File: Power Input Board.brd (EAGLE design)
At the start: 136.7 x 125.3 mm, 17 parts, among them Q1 SPB80P06P

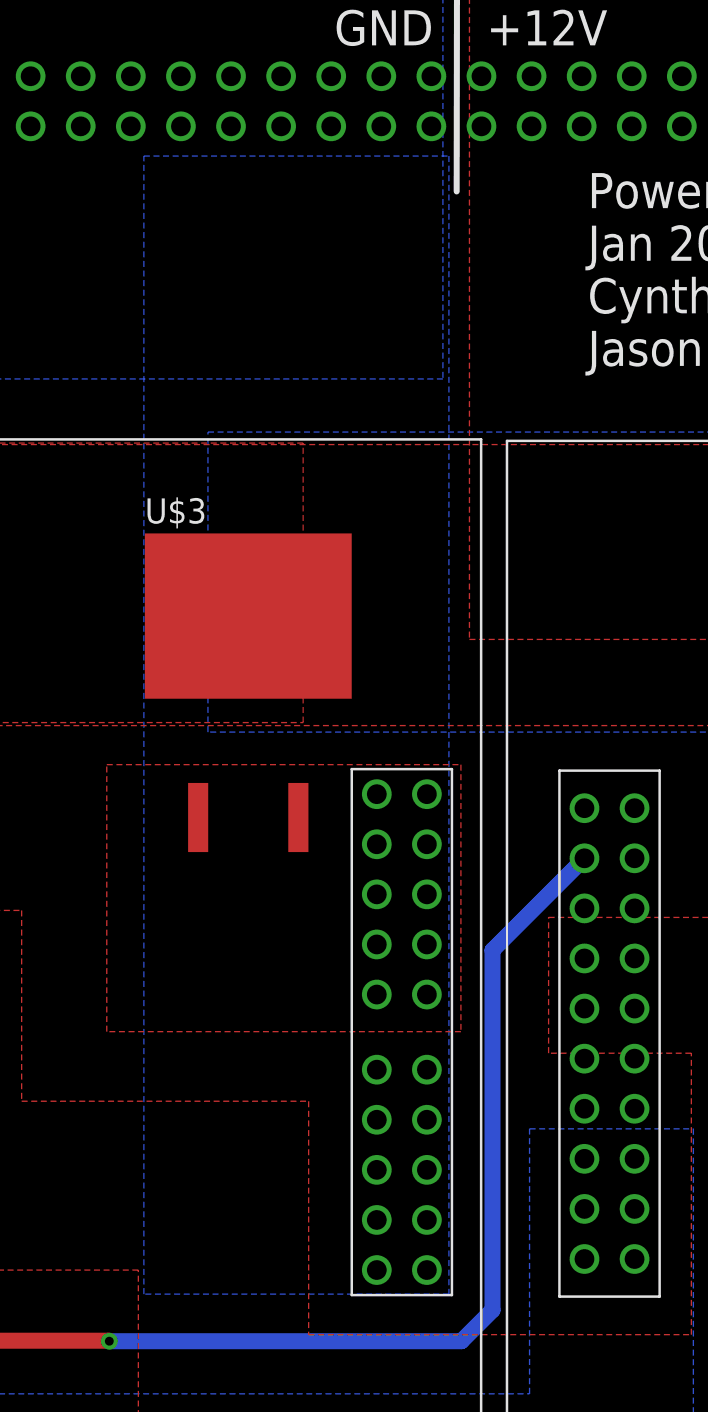
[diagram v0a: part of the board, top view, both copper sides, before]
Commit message: added LED
added LED between 12V and GND
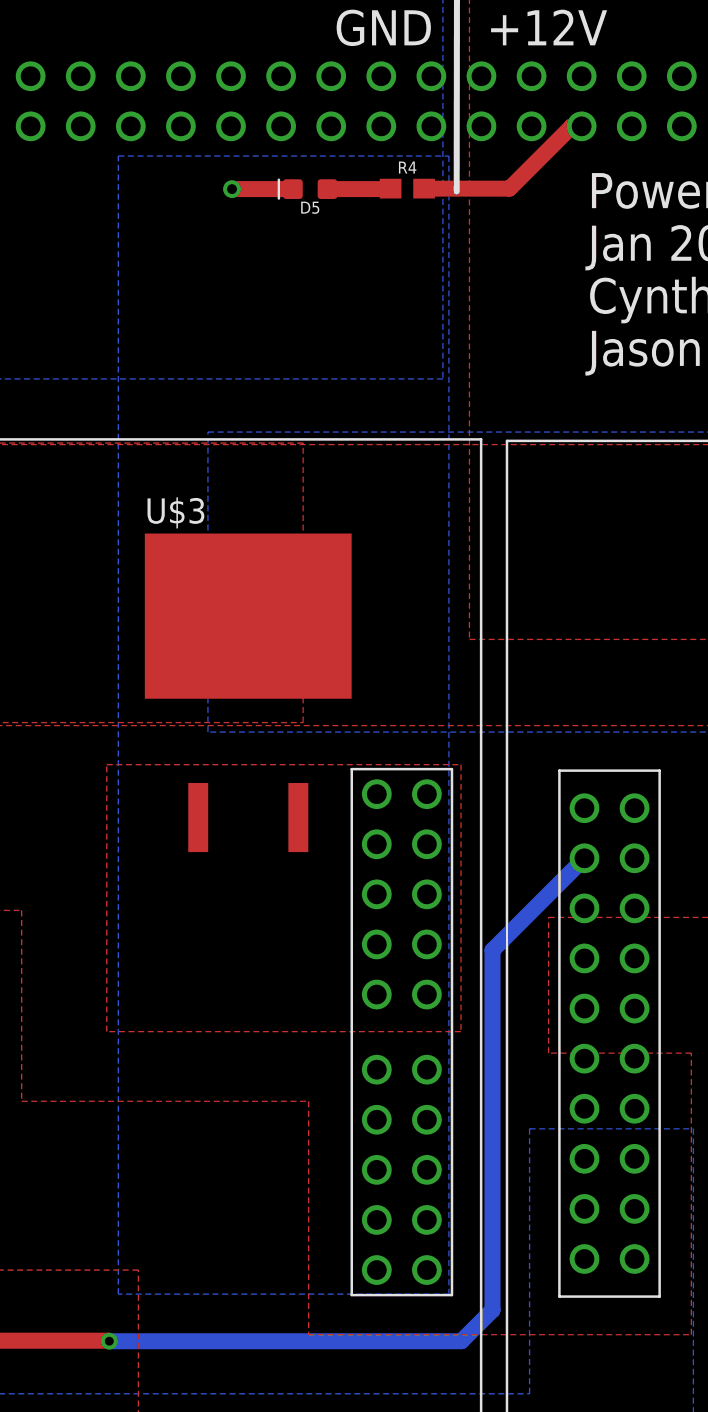
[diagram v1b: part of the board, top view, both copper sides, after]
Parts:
- added D5: (no value), SparkFun-LED:LED-0603
- added R4: 470, SparkFun-Resistors:0603
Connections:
- new net N$4: D5.A, R4.1
- net +12V: now also R4.2
- net GND: now also D5.C
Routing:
- net +12V: track 0.00 -> 9.30 mm
- net N$4: track 0.00 -> 3.21 mm
- net GND: track 0.00 -> 3.09 mm, vias 0 -> 1
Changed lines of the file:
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@@
 </element>
 <element name="U$7" library="PDB_PCB_connectors" package="PDB_PCB_2" value="PDB_PCB_CONNEC" x="0" y="0"/>
+<element name="D5" library="SparkFun-LED" library_urn="urn:adsk.eagle:library:529" package="LED-0603" package3d_urn="urn:adsk.eagle:package:39354/1" value="" x="59.3598" y="110.9472" rot="R180">
+<attribute name="NAME" x="59.3598" y="110.3122" size="0.6096" layer="25" font="vector" ratio="20" rot="R180" align="bottom-center"/>
+<attribute name="VALUE" x="59.3598" y="111.5822" size="0.6096" layer="27" font="vector" ratio="20" rot="R180" align="top-center"/>
+</element>
+<element name="R4" library="SparkFun-Resistors" library_urn="urn:adsk.eagle:library:532" package="0603" package3d_urn="urn:adsk.eagle:package:39650/1" value="470" x="64.2874" y="110.9726">
+<attribute name="NAME" x="64.2874" y="111.7346" size="0.6096" layer="25" font="vector" ratio="20" align="bottom-center"/>
+<attribute name="PROD_ID" value=" " x="64.2874" y="110.9726" size="1.778" layer="27" display="off"/>
+<attribute name="VALUE" x="64.2874" y="109.8296" size="0.6096" layer="27" font="vector" ratio="20" align="top-center"/>
+</element>
 </elements>
 <signals>
@@
 <vertex x="120.777" y="30.5562"/>
 </polygon>
+<contactref element="R4" pad="2"/>
+<wire x1="65.1374" y1="110.9726" x2="69.469" y2="110.9726" width="0.8128" layer="1"/>
+<wire x1="69.469" y1="110.9726" x2="72.6265625" y2="114.1301625" width="0.8128" layer="1"/>
+<wire x1="72.6265625" y1="114.1301625" x2="73.1260375" y2="114.1301625" width="0.8128" layer="1"/>
 </signal>
 <signal name="GND">
@@
 </polygon>
 <polygon width="0.8128" layer="16" isolate="0.8128">
-<vertex x="50.927" y="112.6236"/>
+<vertex x="49.6316" y="112.6236"/>
 <vertex x="66.3956" y="112.6236"/>
 <vertex x="66.3956" y="54.9148"/>
-<vertex x="50.927" y="54.9148"/>
+<vertex x="49.6316" y="54.9148"/>
 </polygon>
 <polygon width="0.8128" layer="16" isolate="0.8128">
@@
 <vertex x="28.0924" y="82.6516"/>
 </polygon>
+<contactref element="D5" pad="C"/>
+<wire x1="58.4828" y1="110.9472" x2="55.3974" y2="110.9472" width="0.8128" layer="1"/>
+<via x="55.3974" y="110.9472" extent="1-16" drill="0.5"/>
 </signal>
 <signal name="N$10">
@@
 </polygon>
 </signal>
+<signal name="N$4">
+<contactref element="D5" pad="A"/>
+<contactref element="R4" pad="1"/>
+<wire x1="60.2368" y1="110.9472" x2="63.412" y2="110.9472" width="0.8128" layer="1"/>
+<wire x1="63.412" y1="110.9472" x2="63.4374" y2="110.9726" width="0.8128" layer="1"/>
+</signal>
 </signals>

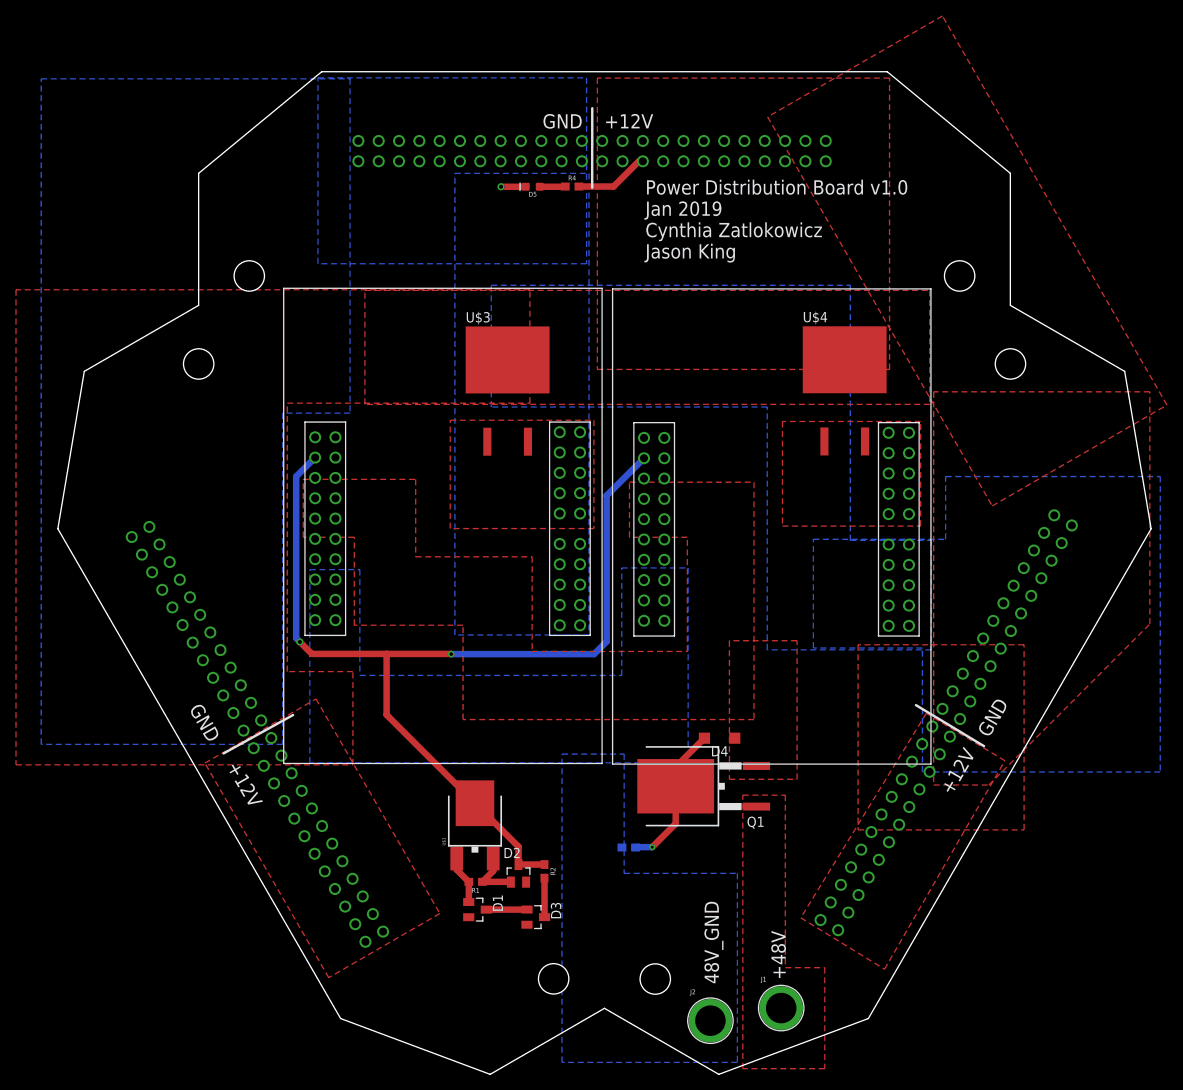
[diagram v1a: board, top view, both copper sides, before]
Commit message: repositioning components
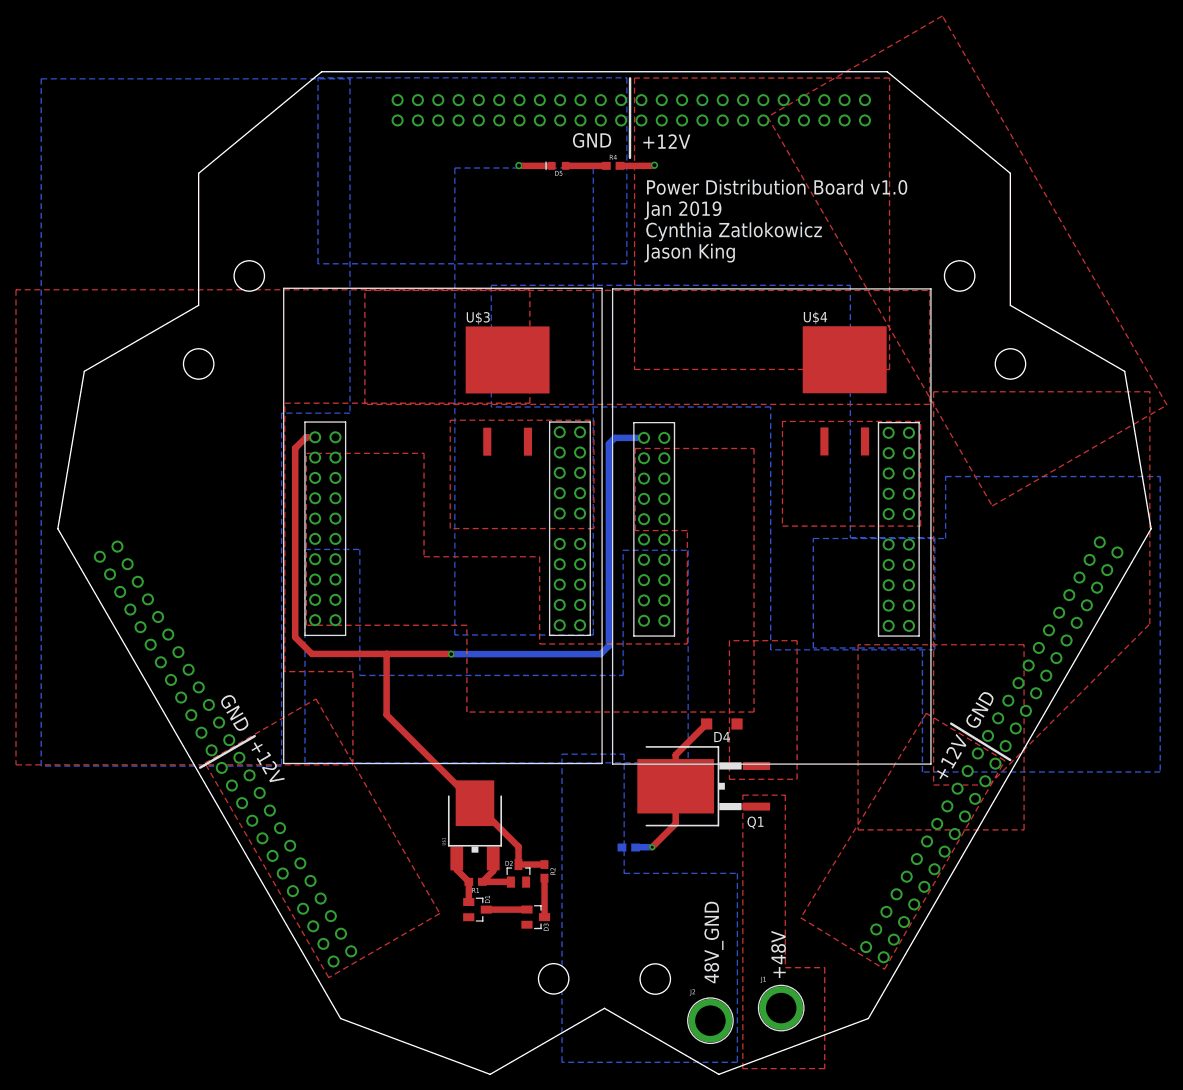
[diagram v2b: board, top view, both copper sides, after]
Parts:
- D1, D3: value (none) -> 22V
- D2: value (none) -> 5V
- D4: value (none) -> 15V
- moved R4 5.75 mm to (69.4, 113.6)
- moved D5 4.17 mm to (62.6, 113.6)
- moved D4 1.80 mm to (83.0, 43.8)
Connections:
- net +48V: now also U$5.+48V5, U$5.+48V6, U$5.+48V7, U$5.+48V8, U$6.+48V5, U$6.+48V6, U$6.+48V7, U$6.+48V8
- net 48V_GND: now also U$5.48V_GND5, U$5.48V_GND6, U$5.48V_GND7, U$5.48V_GND8, U$6.48V_GND5, U$6.48V_GND6, U$6.48V_GND7, U$6.48V_GND8
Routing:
- net ON/OFF: track 125.1 -> 133.5 mm, vias 2 -> 1
- net +12V: track 9.30 -> 4.34 mm, vias 0 -> 1
- net N$3: track 18.4 -> 20.3 mm
- net N$4: track 3.21 -> 5.08 mm
- net GND: track 3.09 -> 4.11 mm
